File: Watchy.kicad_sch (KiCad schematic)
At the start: 72 parts, among them J1 FPC24(0.5MM), J2 USB_C_Receptacle_USB2.0, J3 Battery, M1 Vibration_Motor, Q1 AO3400A, Q2 UMH3N, Q4 CJ2301, Q5 S8050, SW1 BTN, SW2 BTN, SW3 BTN, SW4 BTN, U1 ESP32-PICO-D4, U2 ME6211C33M5G-N, U3 CP2102, U4 BMA423, U5 TP4054, U6 PCF8563BS, Y1 32.768KHz

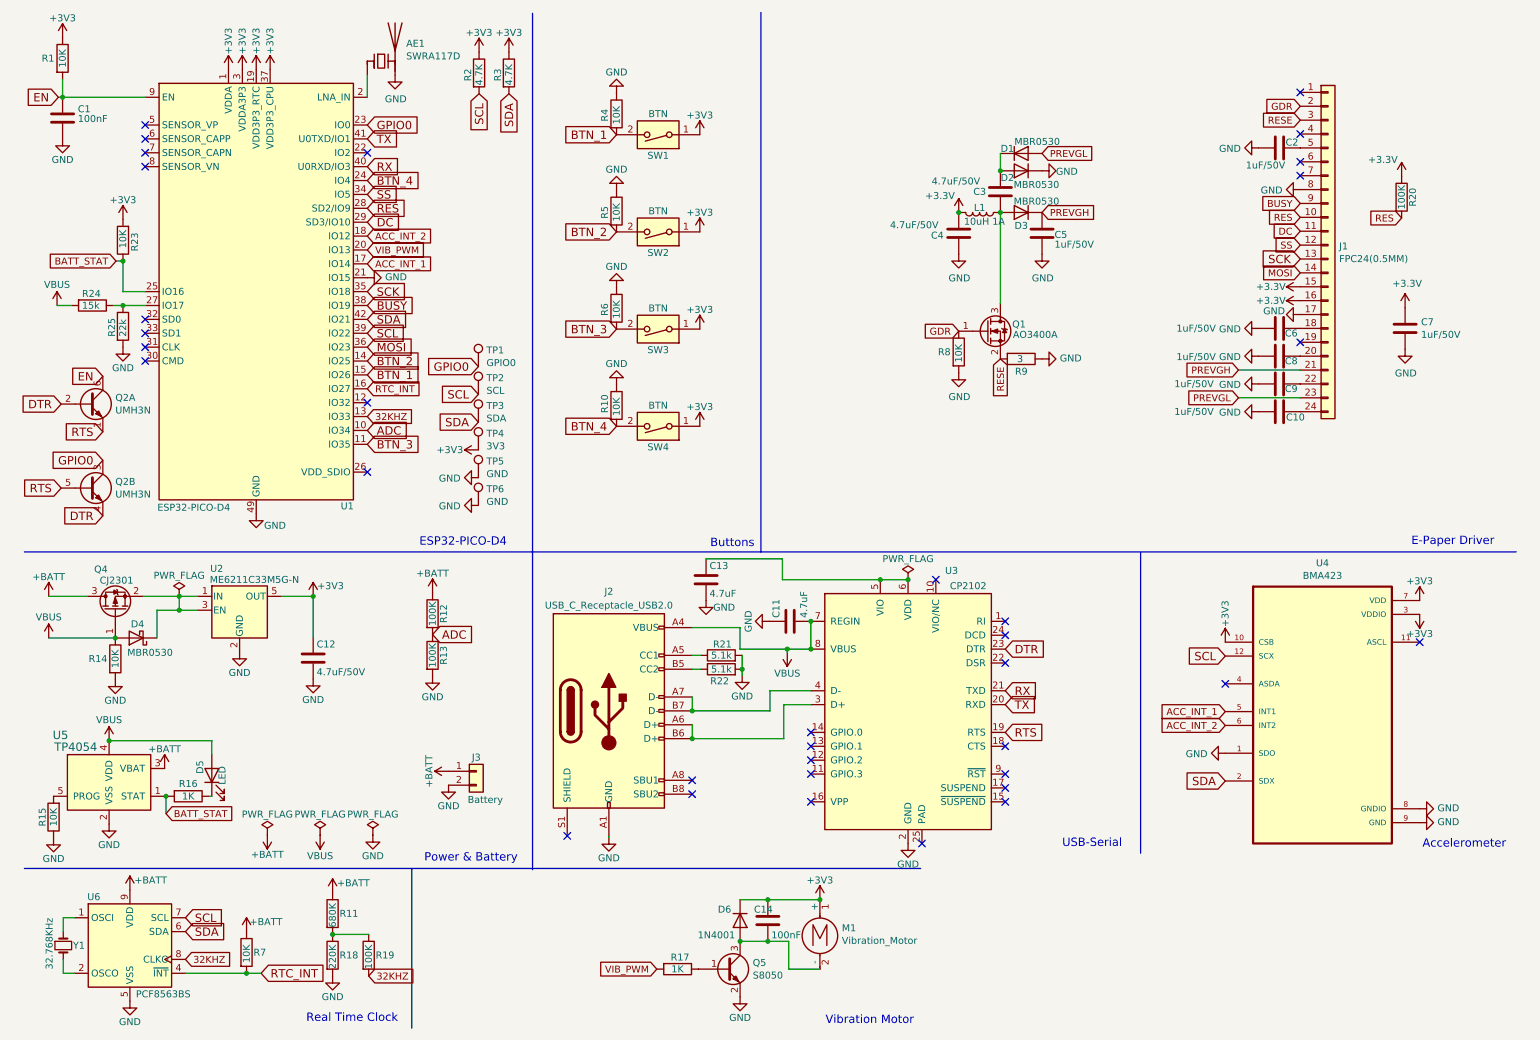
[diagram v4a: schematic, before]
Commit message: use valid pins for charging on gpio pins
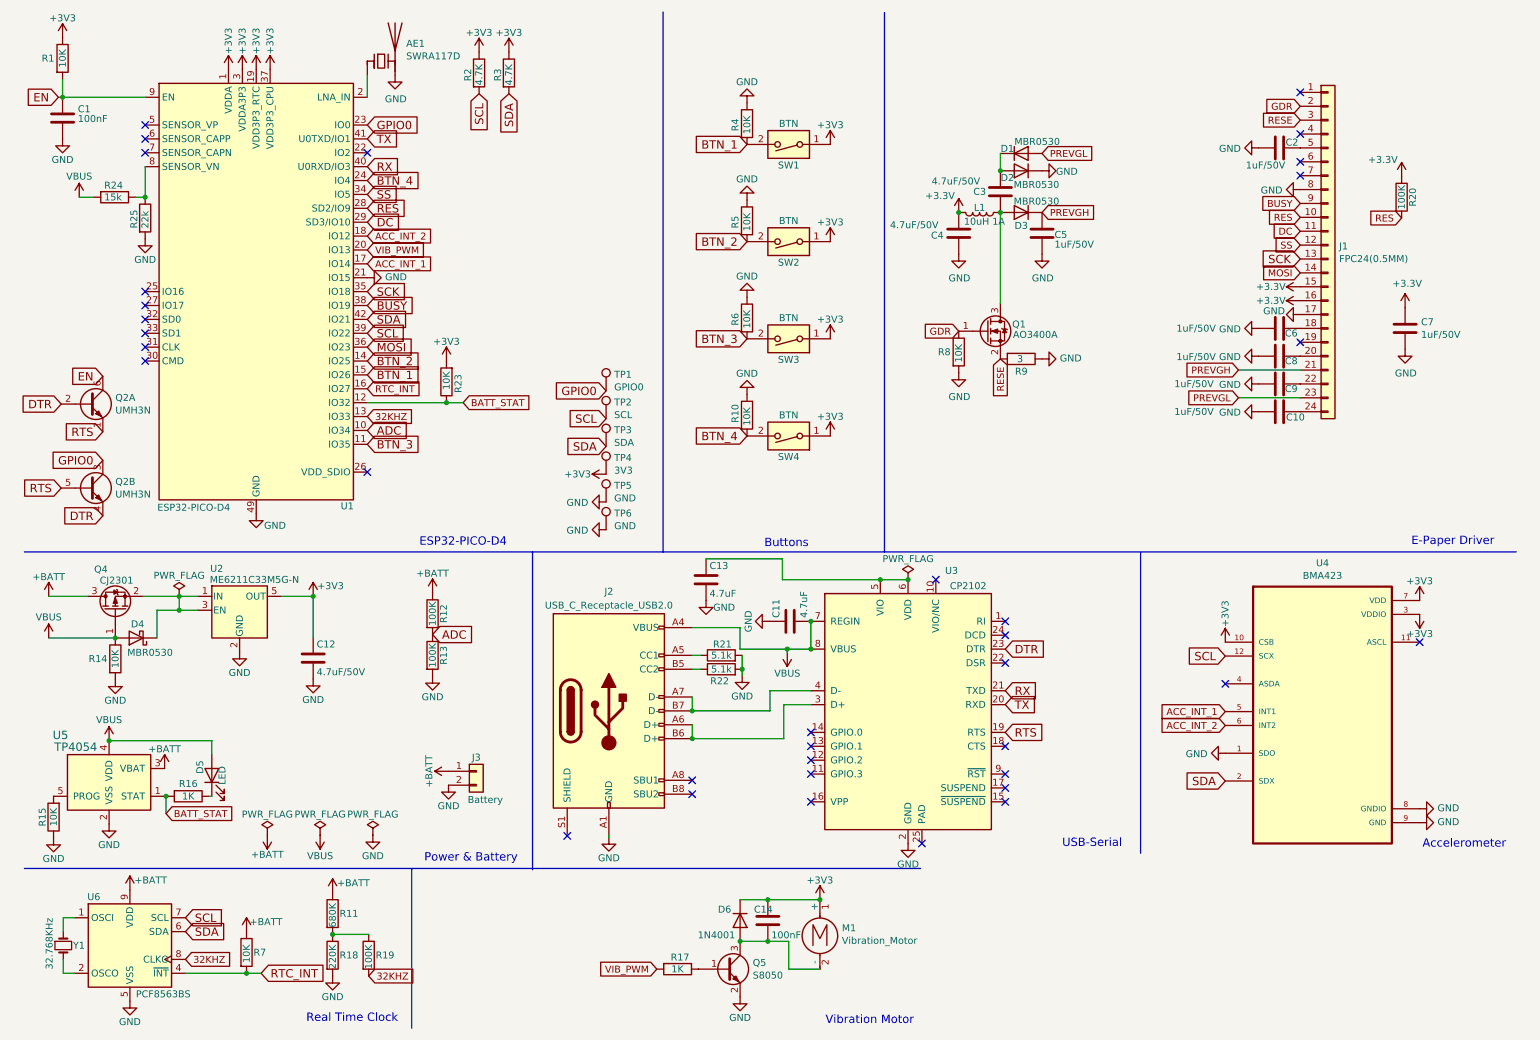
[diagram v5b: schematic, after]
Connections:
- net BATT_STAT: now also U1.12 (IO32); no longer U1.25 (IO16)
- net at R24.1, R25.1: now also U1.8 (SENSOR_VN); no longer U1.27 (IO17)
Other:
- moved on the sheet: R10, R23, R24, R25, R4, R5, R6, SW1, SW2, SW3, SW4, TP1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

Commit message: use watchy footprint for resistors
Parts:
- R21, R22, R23, R24, R25: footprint Resistor_SMD:R_0402_1005Metric -> Watchy:R_0402
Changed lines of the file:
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@@
       (effects (font (size 1.27 1.27)) (justify left))
     )
-    (property "Footprint" "Resistor_SMD:R_0402_1005Metric" (at 139.7 134.112 90)
+    (property "Footprint" "Watchy:R_0402" (at 139.7 134.112 90)
       (effects (font (size 1.27 1.27)) hide)
     )
@@
       (effects (font (size 1.27 1.27)) (justify left))
     )
-    (property "Footprint" "Resistor_SMD:R_0402_1005Metric" (at 139.7 131.572 90)
+    (property "Footprint" "Watchy:R_0402" (at 139.7 131.572 90)
       (effects (font (size 1.27 1.27)) hide)
     )
@@
       (effects (font (size 1.27 1.27)) (justify left))
     )
-    (property "Footprint" "Resistor_SMD:R_0402_1005Metric" (at 32.512 49.784 90)
+    (property "Footprint" "Watchy:R_0402" (at 32.512 49.784 90)
       (effects (font (size 1.27 1.27)) hide)
     )
@@
       (effects (font (size 1.27 1.27)) (justify left))
     )
-    (property "Footprint" "Resistor_SMD:R_0402_1005Metric" (at 28.702 44.196 90)
+    (property "Footprint" "Watchy:R_0402" (at 28.702 44.196 90)
       (effects (font (size 1.27 1.27)) hide)
     )
@@
       (effects (font (size 1.27 1.27)) (justify left))
     )
-    (property "Footprint" "Resistor_SMD:R_0402_1005Metric" (at 91.186 79.756 90)
-      (effects (font (size 1.27 1.27)) hide)
-    )
+    (property "Footprint" "Watchy:R_0402" (at 91.186 79.756 90)
+      (effects (font (size 1.27 1.27)) hide)
+    )

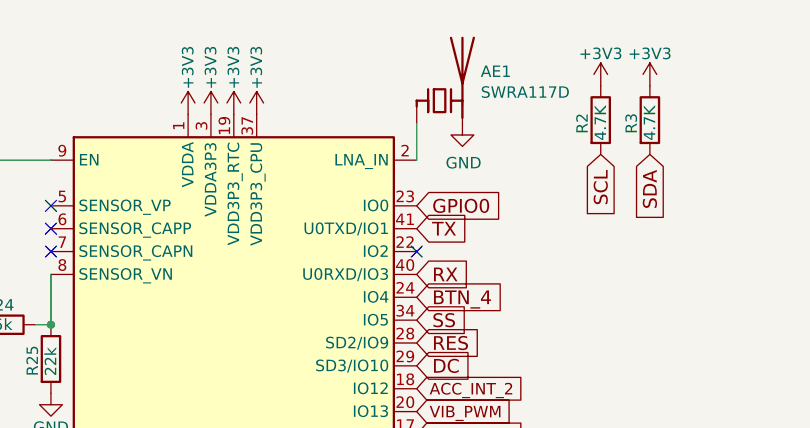
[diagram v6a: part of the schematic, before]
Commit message: erstes Layout, buttons fehlen
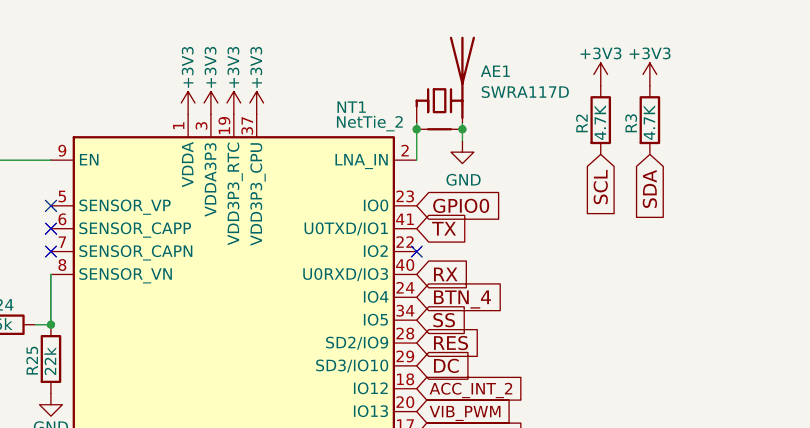
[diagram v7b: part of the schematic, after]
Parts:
- added NT1: NetTie_2, symbol Device:NetTie_2
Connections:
- net GND: now also NT1.2
- net at AE1.1 (FEED), U1.2 (LNA_IN): now also NT1.1
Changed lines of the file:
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@@
   (junction (at 68.58 180.848) (diameter 0) (color 0 0 0 0)
   )
+  (junction (at 80.01 24.257) (diameter 0) (color 0 0 0 0)
+  )
   (junction (at 40.513 118.999) (diameter 0) (color 0 0 0 0)
   )
@@
   (junction (at 19.177 27.686) (diameter 0) (color 0 0 0 0)
   )
+  (junction (at 74.93 24.257) (diameter 0) (color 0 0 0 0)
+  )
   (junction (at 151.765 128.651) (diameter 0) (color 0 0 0 0)
   )
@@
     (stroke (width 0) (type default))
   )
+  (wire (pts (xy 80.01 24.257) (xy 80.01 23.622))
+    (stroke (width 0) (type default))
+  )
   (wire (pts (xy 136.906 112.141) (xy 150.876 112.141))
     (stroke (width 0) (type default))
   )
+  (wire (pts (xy 74.93 24.257) (xy 74.93 23.622))
+    (stroke (width 0) (type default))
+  )
   (wire (pts (xy 143.129 124.714) (xy 143.129 128.651))
     (stroke (width 0) (type default))
@@
     (stroke (width 0) (type default))
   )
-  (wire (pts (xy 74.93 27.686) (xy 74.93 23.622))
+  (wire (pts (xy 74.93 27.686) (xy 74.93 24.257))
     (stroke (width 0) (type default))
   )
@@
     (stroke (width 0) (type default))
   )
+  (wire (pts (xy 80.01 25.527) (xy 80.01 24.257))
+    (stroke (width 0) (type default))
+  )
   (wire (pts (xy 75.184 180.848) (xy 68.58 180.848))
     (stroke (width 0) (type default))
@@
     )
   )
-  (symbol (lib_id "power:GND") (at 80.01 23.622 0) (unit 1)
+  (symbol (lib_id "power:GND") (at 80.01 25.527 0) (unit 1)
     (in_bom yes) (on_board yes) (dnp no)
-    (property "Reference" "#PWR08" (at 80.01 29.972 0)
+    (property "Reference" "#PWR08" (at 80.01 31.877 0)
       (effects (font (size 1.27 1.27)) hide)
     )
-    (property "Value" "GND" (at 80.137 28.0162 0)
+    (property "Value" "GND" (at 80.137 29.9212 0)
       (effects (font (size 1.27 1.27)))
     )
-    (property "Footprint" "" (at 80.01 23.622 0)
+    (property "Footprint" "" (at 80.01 25.527 0)
       (effects (font (size 1.27 1.27)) hide)
     )
-    (property "Datasheet" "" (at 80.01 23.622 0)
+    (property "Datasheet" "" (at 80.01 25.527 0)
       (effects (font (size 1.27 1.27)) hide)
     )
@@
         )
       )
+    )
+  )
+  (symbol (lib_id "Device:NetTie_2") (at 77.47 24.257 0) (unit 1)
+    (in_bom no) (on_board yes) (dnp no)
+    (property "Reference" "NT1" (at 67.691 21.844 0)
+      (effects (font (size 1.27 1.27)))
+    )
+    (property "Value" "NetTie_2" (at 69.723 23.495 0)
+      (effects (font (size 1.27 1.27)))
+    )
+    (property "Footprint" "" (at 77.47 24.257 0)
+      (effects (font (size 1.27 1.27)) hide)
+    )
+    (property "Datasheet" "~" (at 77.47 24.257 0)
+      (effects (font (size 1.27 1.27)) hide)
+    )
+    (pin "1")
+    (pin "2")
+    (instances
+      (project "Watchy"
+        (path "/4168ccf9-7940-46a9-babd-bad8c703bb50"
+          (reference "NT1") (unit 1)
+        )
+      )

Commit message: Gerbers erstellt
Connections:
- net GND: now also U3.25 (PAD)
- no-connect marks 35 -> 34
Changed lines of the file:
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@@
   (junction (at 134.366 145.034) (diameter 0) (color 0 0 0 0)
+  )
+  (junction (at 173.863 164.846) (diameter 0) (color 0 0 0 0)
   )
   (junction (at 173.863 115.951) (diameter 0) (color 0 0 0 0)
@@
   (no_connect (at 156.083 146.431))
   (no_connect (at 191.643 131.191))
-  (no_connect (at 176.403 164.211))
   (no_connect (at 245.618 39.497))
   (no_connect (at 156.083 151.511))
@@
     (stroke (width 0) (type default))
   )
+  (wire (pts (xy 173.863 164.846) (xy 173.863 164.211))
+    (stroke (width 0) (type default))
+  )
   (wire (pts (xy 152.019 182.118) (xy 152.019 187.198))
     (stroke (width 0) (type default))
@@
     (stroke (width 0) (type default))
   )
+  (wire (pts (xy 176.403 164.211) (xy 176.403 164.846))
+    (stroke (width 0) (type default))
+  )
   (wire (pts (xy 134.366 142.494) (xy 134.366 145.034))
     (stroke (width 0) (type default))
@@
     (stroke (width 0) (type default))
   )
+  (wire (pts (xy 176.403 164.846) (xy 173.863 164.846))
+    (stroke (width 0) (type default))
+  )
   (wire (pts (xy 143.51 132.334) (xy 143.51 133.477))
     (stroke (width 0) (type default))
@@
   )
   (polyline (pts (xy 83.058 168.783) (xy 83.058 197.993))
+    (stroke (width 0) (type default))
+  )
+  (wire (pts (xy 173.863 165.608) (xy 173.863 164.846))
     (stroke (width 0) (type default))
   )
@@
     )
   )
-  (symbol (lib_id "power:GND") (at 173.863 164.211 0) (unit 1)
-    (in_bom yes) (on_board yes) (dnp no)
-    (property "Reference" "#PWR060" (at 173.863 170.561 0)
-      (effects (font (size 1.27 1.27)) hide)
-    )
-    (property "Value" "GND" (at 173.863 168.021 0)
-      (effects (font (size 1.27 1.27)))
-    )
-    (property "Footprint" "" (at 173.863 164.211 0)
-      (effects (font (size 1.27 1.27)) hide)
-    )
-    (property "Datasheet" "" (at 173.863 164.211 0)
-      (effects (font (size 1.27 1.27)) hide)
-    )
+  (symbol (lib_id "power:GND") (at 173.863 165.608 0) (unit 1)
+    (in_bom yes) (on_board yes) (dnp no)
+    (property "Reference" "#PWR060" (at 173.863 171.958 0)
+      (effects (font (size 1.27 1.27)) hide)
+    )
+    (property "Value" "GND" (at 173.863 169.418 0)
+      (effects (font (size 1.27 1.27)))
+    )
+    (property "Footprint" "" (at 173.863 165.608 0)
+      (effects (font (size 1.27 1.27)) hide)
+    )
+    (property "Datasheet" "" (at 173.863 165.608 0)
+      (effects (font (size 1.27 1.27)) hide)
+    )
